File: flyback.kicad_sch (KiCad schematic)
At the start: 16 parts, among them Q1 IPD050N10N5, Q2 IPD050N10N5, T1 MSD1514-103ME

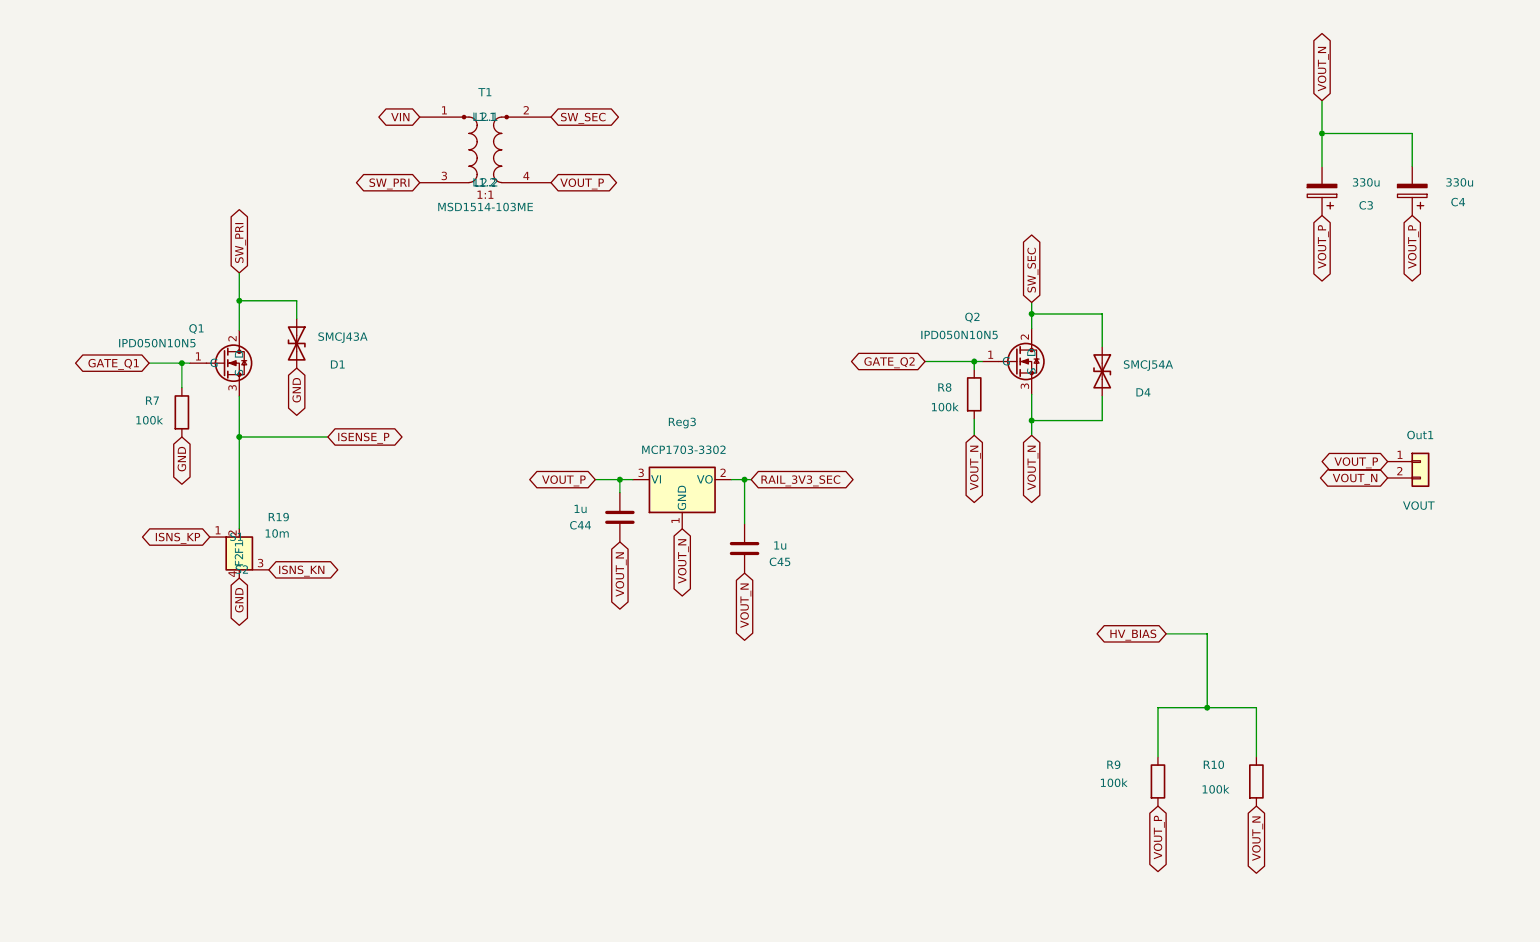
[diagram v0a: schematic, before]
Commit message: Retire la barriere d'isolation primaire/secondaire (secondaire non isole du primaire dans le montage final)
Decision utilisateur du 2026-10-25 : le secondaire de puissance (VOUT_N/
VOUT_P) ne sera plus flottant ni isole galvaniquement du primaire. La
regle .kicad_dru barriere_primaire_secondaire est retiree (commentee,
pas supprimee), la classe de nets SEC est conservee a titre
organisationnel dans KICAD-HT.kicad_pro. Seule la barriere controle
(C2000) <-> puissance reste une isolation reelle. 00-intention-conception.md,
README.md et doc/plan-isolation-4couches.md mis a jour (section 20bis).
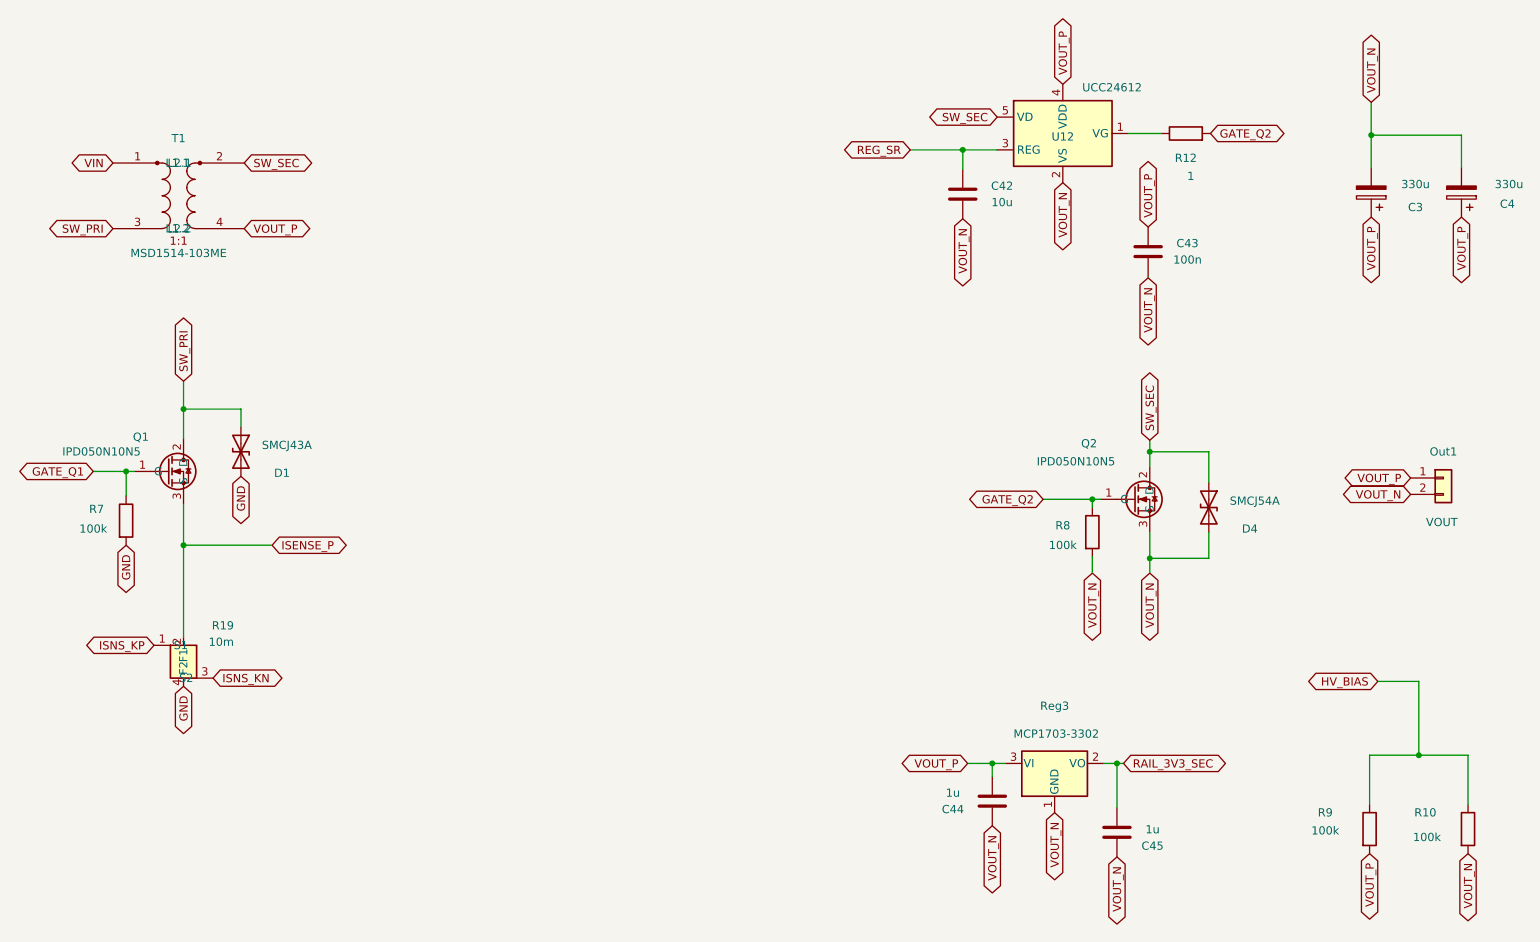
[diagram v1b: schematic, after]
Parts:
- added C42: 10u, Capacitor_SMD:C_0805_2012Metric, symbol Device:C
- added C43: 100n, Capacitor_SMD:C_0805_2012Metric, symbol Device:C
- added R12: 1, Resistor_SMD:R_0805_2012Metric, symbol Device:R
- added U12: UCC24612, Package_TO_SOT_SMD:SOT-23-5, symbol custom_parts:UCC24612
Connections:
- net GATE_Q2: now also R12.2
- net SW_SEC: now also U12.5 (VD)
- net VOUT_N: now also C42.1, C43.1, U12.2 (VS)
- net VOUT_P: now also C43.2, U12.4 (VDD)
- new net: R12.1, U12.1 (VG)
- new net REG_SR: C42.2, U12.3 (REG)
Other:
- moved on the sheet: C3, C4, C44, C45, D1, D4, Out1, Q1, Q2, R10, R19, R7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
